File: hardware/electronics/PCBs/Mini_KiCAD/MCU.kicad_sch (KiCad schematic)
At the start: 13 parts, among them J3 HEADER2, U1 ATMEGA32U4RC-AU

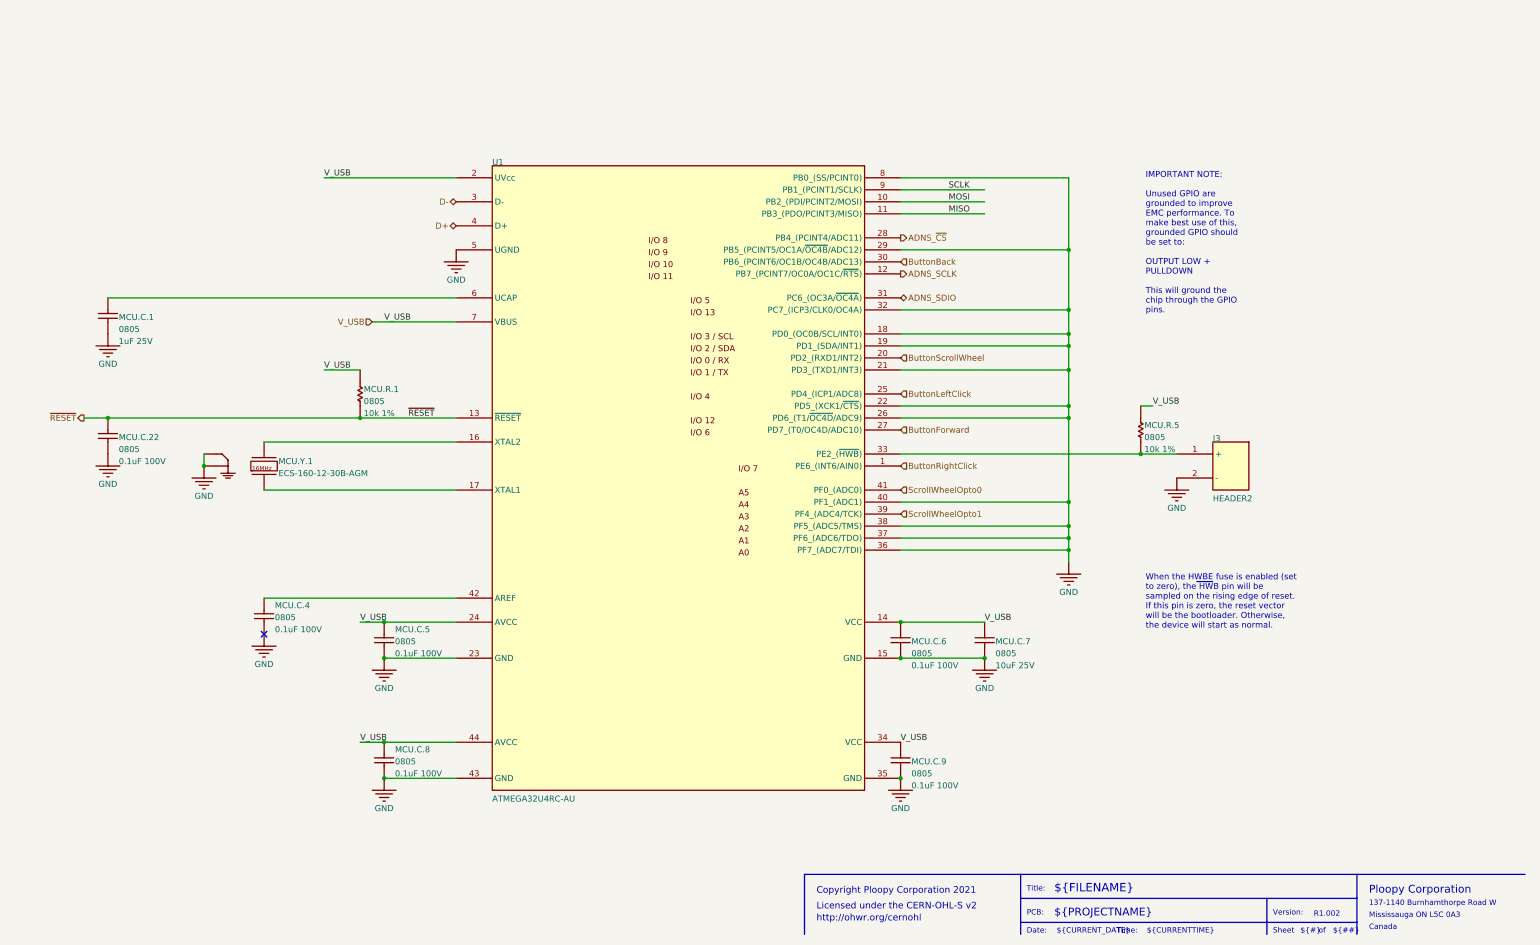
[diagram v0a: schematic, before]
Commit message: Initial commit of the modified Ploopy Mini PCB with RP2040, PMW3360 and mid-mounted USB-C
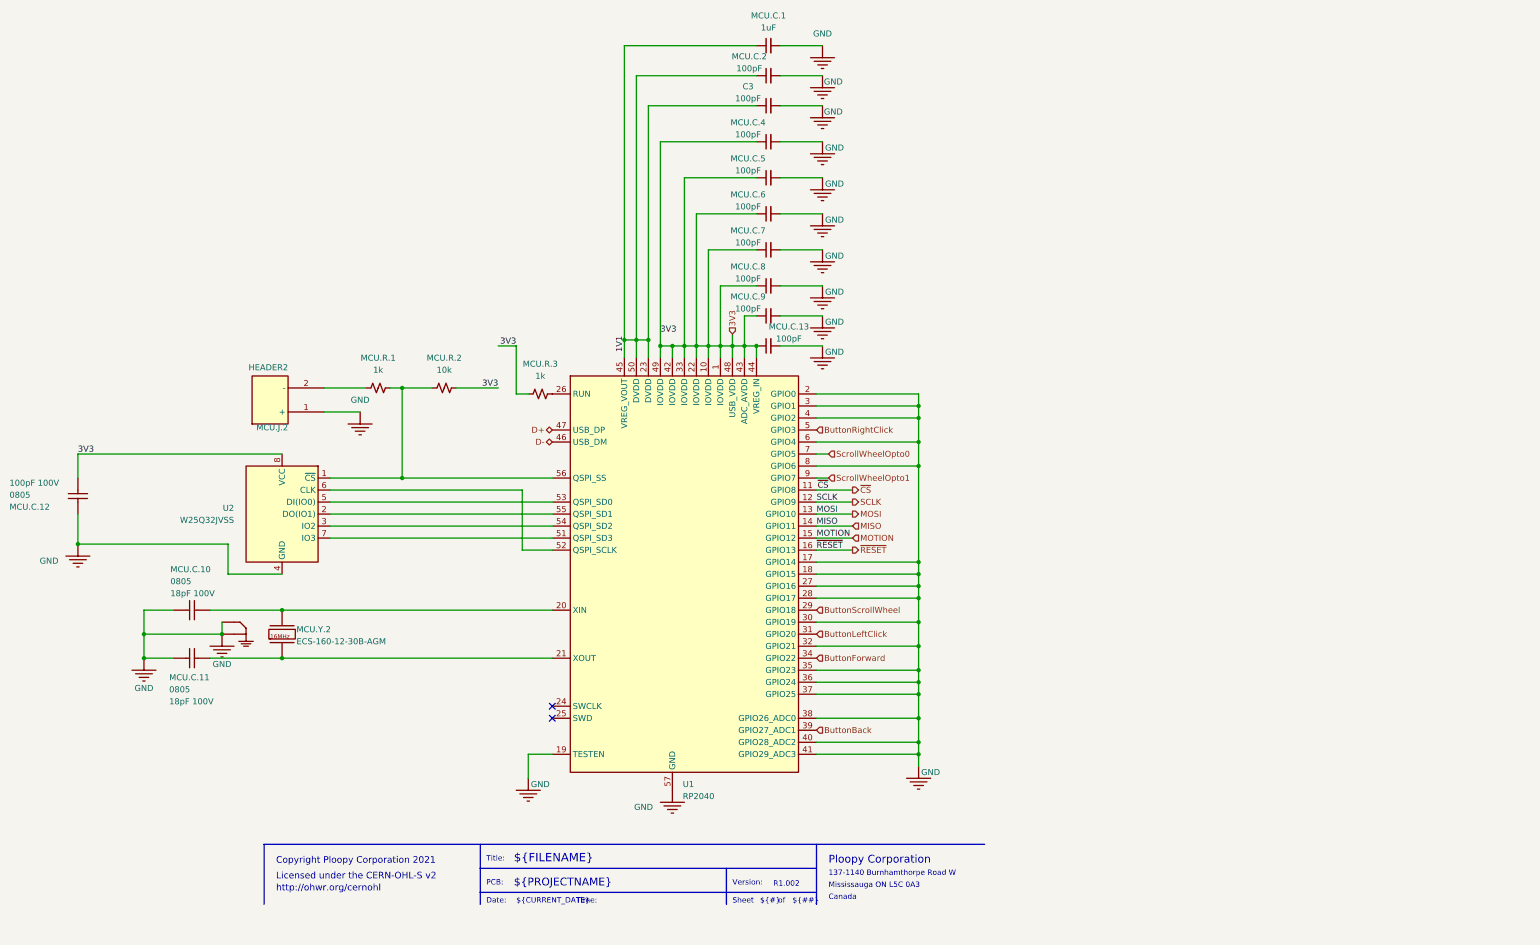
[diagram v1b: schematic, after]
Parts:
- removed J3: HEADER2, 2x1, symbol Mini-altium-import:MCU_0_HEADER2
- removed MCU.C.1: 0805, 0805 - TALL, symbol Mini-altium-import:MCU_1_Cap 1uF 25V
- removed MCU.C.22, MCU.C.4, MCU.C.5, MCU.C.8, MCU.C.9: 0805, 0805 - TALL, symbol Mini-altium-import:MCU_1_Cap 0.1uF 100V
- removed MCU.C.6: 0805, 0805 - TALL, symbol Mini-altium-import:MCU_1_mirrored_Cap 0.1uF 100V
- removed MCU.C.7: 0805, 0805 - TALL, symbol Mini-altium-import:MCU_1_mirrored_Cap 10uF 25V
- removed MCU.R.1, MCU.R.5: 0805, 0805, symbol Mini-altium-import:MCU_1_Res 10k 1% 0805
- removed MCU.Y.1: ECS-160-12-30B-AGM, LFXTAL055663BULK, symbol Mini-altium-import:MCU_0_ECS-160-12-30B-AGM
- removed U1: ATMEGA32U4RC-AU, ATmega32U4 - TQFP80P1200X1200X120-44N, symbol Mini-altium-import:MCU_0_ATMEGA32U4RC-AU
- added C3, MCU.C.13, MCU.C.2, MCU.C.4, MCU.C.5, MCU.C.6, MCU.C.7, MCU.C.8, MCU.C.9: 100pF, Chip_Passives.PcbLib:0805, symbol Device:C_Small
- added MCU.C.1: 1uF, Chip_Passives.PcbLib:0805, symbol Device:C_Small
- added MCU.C.10, MCU.C.11, MCU.C.12: 0805, Chip_Passives.PcbLib:0805 - TALL, symbol Mini-altium-import:MCU_1_Cap 0.1uF 100V
- added MCU.J.2: HEADER2, Connectors.PcbLib:2x1, symbol Mini-altium-import:MCU_0_HEADER2
- added MCU.R.1, MCU.R.3: 1k, Chip_Passives.PcbLib:0805, symbol Device:R_Small_US
- added MCU.R.2: 10k, Chip_Passives.PcbLib:0805, symbol Device:R_Small_US
- added MCU.Y.2: ECS-160-12-30B-AGM, Crystals.PcbLib:LFXTAL055663BULK, symbol Mini-altium-import:MCU_0_ECS-160-12-30B-AGM
- added U1: RP2040, Package_DFN_QFN:QFN-56-1EP_7x7mm_P0.4mm_EP3.2x3.2mm, symbol MCU_RaspberryPi:RP2040
- added U2: W25Q32JVSS, Package_SO:SOIC-8_5.23x5.23mm_P1.27mm, symbol Memory_Flash:W25Q32JVSS
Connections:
- net ButtonBack: now also U1.39 (GPIO27_ADC1)
- net ButtonForward: now also U1.34 (GPIO22)
- net ButtonLeftClick: now also U1.31 (GPIO20)
- net ButtonRightClick: now also U1.5 (GPIO3)
- net ButtonScrollWheel: now also U1.29 (GPIO18)
- net D+: now also U1.47 (USB_DP)
- net D-: now also U1.46 (USB_DM)
- net GND: now also C3.2, MCU.C.1.2, MCU.C.10.1, MCU.C.11.1, MCU.C.12.1, MCU.C.13.2, MCU.C.2.2, MCU.C.4.2, MCU.C.5.2, MCU.C.6.2, MCU.C.7.2, MCU.C.8.2, MCU.C.9.2, MCU.J.2.1 (+), MCU.Y.2.2, MCU.Y.2.4, U1.17 (GPIO14), U1.18 (GPIO15), U1.19 (TESTEN), U1.2 (GPIO0), U1.27 (GPIO16), U1.28 (GPIO17), U1.3 (GPIO1), U1.30 (GPIO19), U1.32 (GPIO21), U1.35 (GPIO23), U1.36 (GPIO24), U1.37 (GPIO25), U1.38 (GPIO26_ADC0), U1.4 (GPIO2), U1.40 (GPIO28_ADC2), U1.41 (GPIO29_ADC3), U1.57 (GND), U1.6 (GPIO4), U1.8 (GPIO6), U2.4 (GND)
- net MISO: now also U1.14 (GPIO11)
- net MOSI: now also U1.13 (GPIO10)
- net SCLK: now also U1.12 (GPIO9)
- net ScrollWheelOpto0: now also U1.7 (GPIO5)
- net ScrollWheelOpto1: now also U1.9 (GPIO7)
- net ~{RESET}: now also U1.16 (GPIO13)
- new net: MCU.R.3.2, U1.26 (RUN)
- new net: MCU.C.10.2, MCU.Y.2.1, U1.20 (XIN)
- new net: MCU.C.11.2, MCU.Y.2.3, U1.21 (XOUT)
- new net: MCU.R.1.2, MCU.R.2.1, U1.56 (QSPI_SS), U2.1 (~{CS})
- new net: U1.55 (QSPI_SD1), U2.2 (DO(IO1))
- new net: U1.54 (QSPI_SD2), U2.3 (IO2)
- new net: U1.53 (QSPI_SD0), U2.5 (DI(IO0))
- new net: U1.52 (QSPI_SCLK), U2.6 (CLK)
- new net: U1.51 (QSPI_SD3), U2.7 (IO3)
- new net: MCU.J.2.2 (-), MCU.R.1.1
- new net 1V1: C3.1, MCU.C.1.1, MCU.C.2.1, U1.23 (DVDD), U1.45 (VREG_VOUT), U1.50 (DVDD)
- new net 3V3: MCU.C.12.2, MCU.C.13.1, MCU.C.4.1, MCU.C.5.1, MCU.C.6.1, MCU.C.7.1, MCU.C.8.1, MCU.C.9.1, MCU.R.2.2, MCU.R.3.1, U1.1 (IOVDD), U1.10 (IOVDD), U1.22 (IOVDD), U1.33 (IOVDD), U1.42 (IOVDD), U1.43 (ADC_AVDD), U1.44 (VREG_IN), U1.48 (USB_VDD), U1.49 (IOVDD), U2.8 (VCC)
- new net MOTION: U1.15 (GPIO12)
- new net ~{CS}: U1.11 (GPIO8)
- no-connect marks 1 -> 2
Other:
- note removed: "${CURRENTTIME}"

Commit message: Fixed SPI pin assignment, capacitor values and added the missing resistor for the crystal
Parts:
- added MCU.R.4: 1k, Chip_Passives.PcbLib:0805, symbol Device:R_Small_US
- MCU.C.13: value 100pF -> 1uf
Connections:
- net GND: now also U1.11 (GPIO8), U1.13 (GPIO10); no longer U1.2 (GPIO0), U1.4 (GPIO2)
- net MISO: now also U1.2 (GPIO0); no longer U1.14 (GPIO11)
- net MOSI: now also U1.9 (GPIO7); no longer U1.13 (GPIO10)
- net SCLK: now also U1.4 (GPIO2); no longer U1.12 (GPIO9)
- net ScrollWheelOpto0: now also U1.14 (GPIO11); no longer U1.7 (GPIO5)
- net ScrollWheelOpto1: now also U1.12 (GPIO9); no longer U1.9 (GPIO7)
- net ~{CS}: now also U1.7 (GPIO5); no longer U1.11 (GPIO8)
- net at MCU.C.11.2, MCU.Y.2.3: now also MCU.R.4.1; no longer U1.21 (XOUT)
- new net: MCU.R.4.2, U1.21 (XOUT)

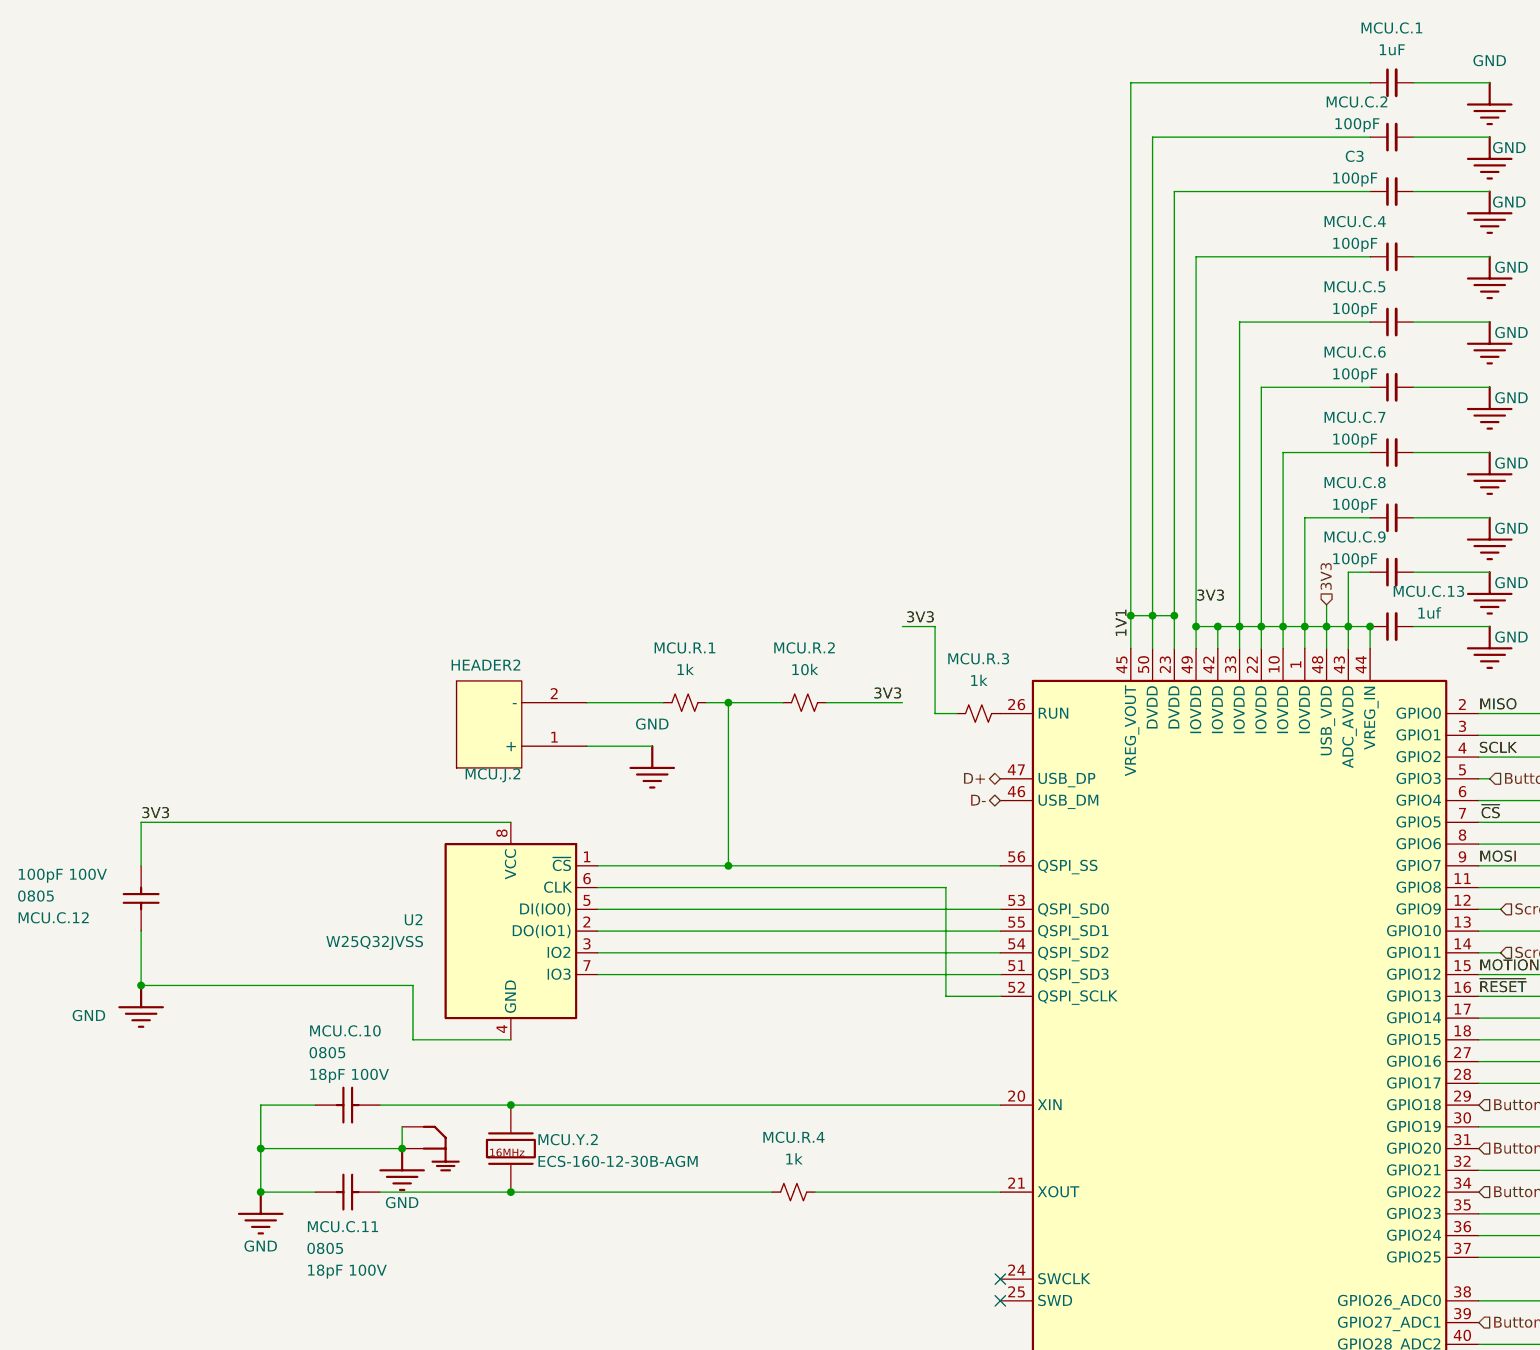
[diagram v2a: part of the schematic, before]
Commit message: Fixed crystal and capacitor values
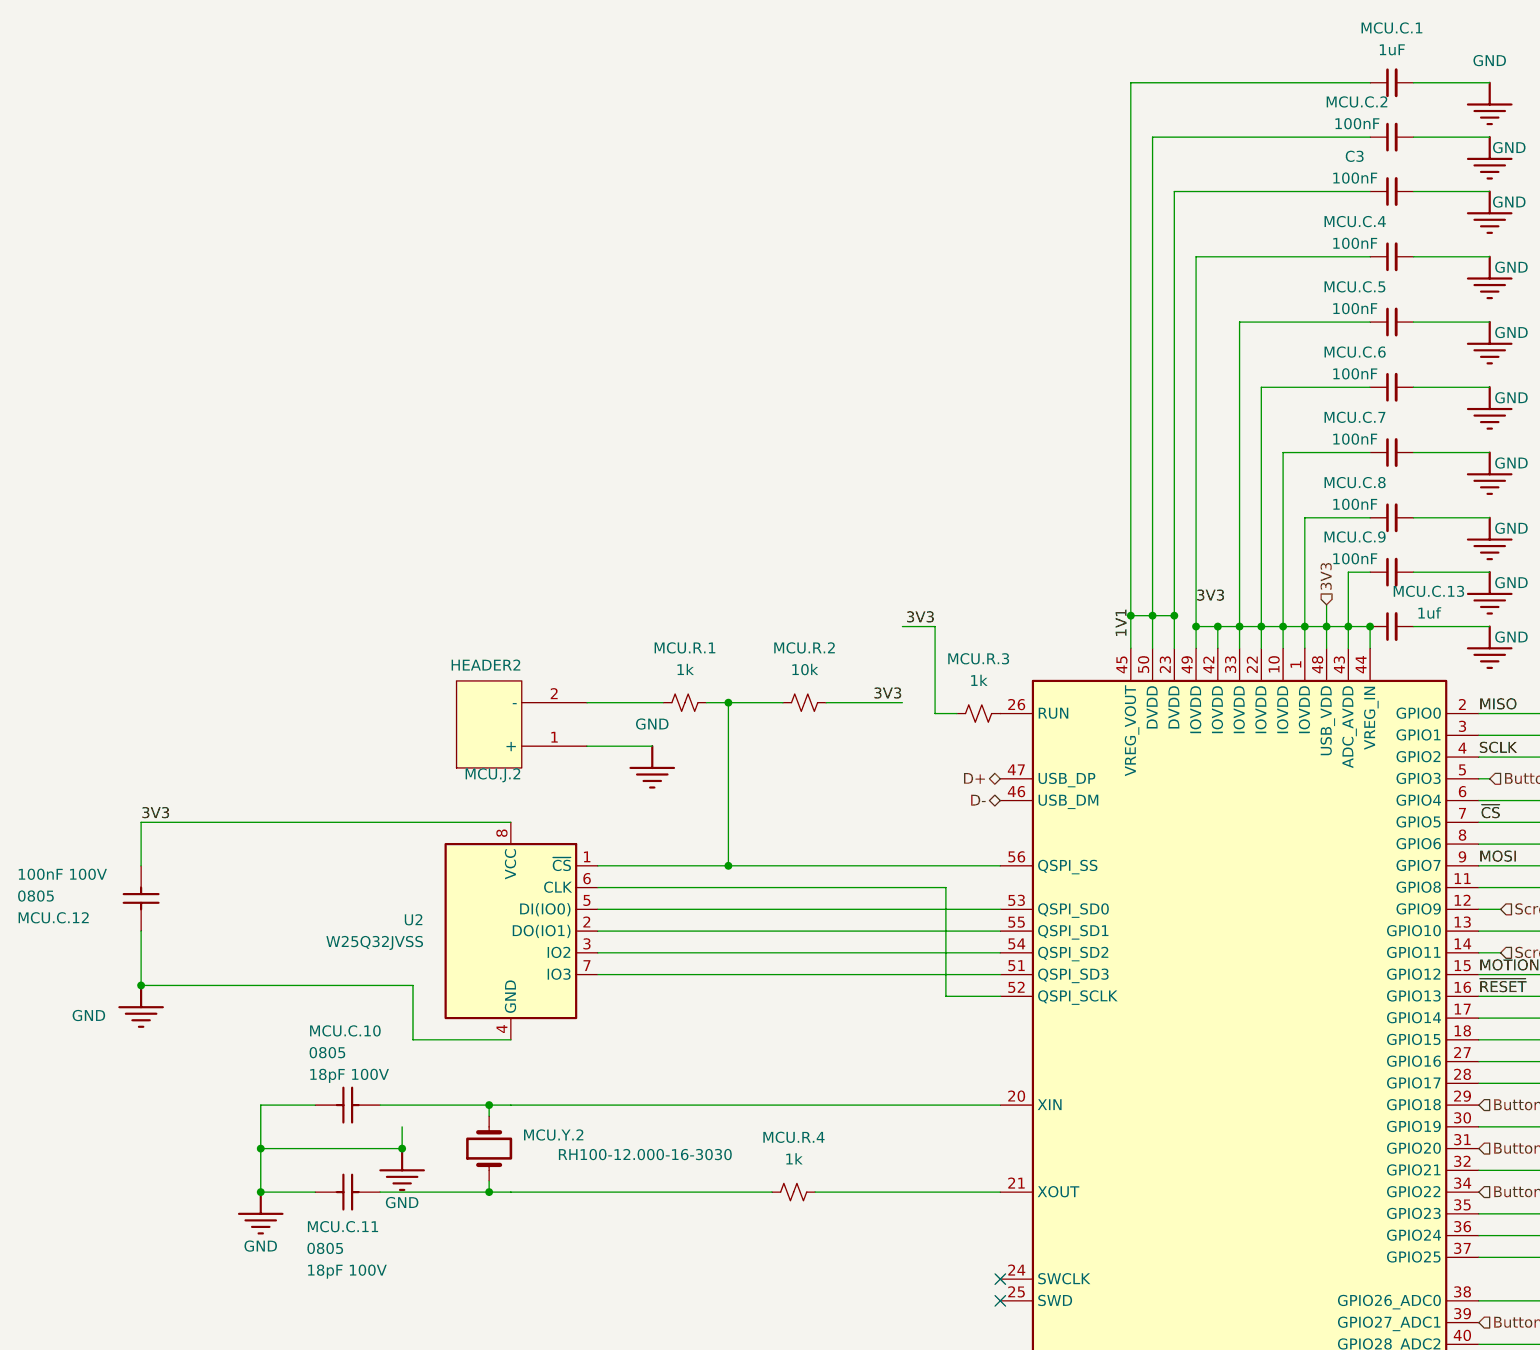
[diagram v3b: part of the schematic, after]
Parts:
- C3, MCU.C.2, MCU.C.4, MCU.C.5, MCU.C.6, MCU.C.7, MCU.C.8, MCU.C.9: value 100pF -> 100nF
- MCU.C.12: ALTIUM_VALUE 100pF 100V -> 100nF 100V
- MCU.Y.2: value ECS-160-12-30B-AGM -> RH100-12.000-16-3030; symbol Mini-altium-import:MCU_0_ECS-160-12-30B-AGM -> Device:Crystal
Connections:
- net GND: no longer MCU.Y.2.2, MCU.Y.2.4
- net at MCU.C.10.2, U1.20 (XIN): now also MCU.Y.2.2; no longer MCU.Y.2.1
- net at MCU.C.11.2, MCU.R.4.1: now also MCU.Y.2.1; no longer MCU.Y.2.3
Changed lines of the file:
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@@
 	)
 	(junction
+		(at 85.09 142.24)
+		(diameter 0)
+		(color 0 0 0 0)
+	)
+	(junction
 		(at 187.96 86.36)
 		(diameter 0)
@@
 	)
 	(junction
-		(at 87.63 142.24)
-		(diameter 0)
-		(color 0 0 0 0)
-	)
-	(junction
 		(at 222.25 139.7)
 		(diameter 0)
@@
 	)
 	(junction
-		(at 222.25 144.78)
+		(at 85.09 152.4)
 		(diameter 0)
 		(color 0 0 0 0)
 	)
 	(junction
-		(at 87.63 152.4)
+		(at 222.25 144.78)
 		(diameter 0)
 		(color 0 0 0 0)
@@
 	(wire
 		(pts
+			(xy 85.09 151.13) (xy 85.09 152.4)
+		)
+		(stroke
+			(width 0)
+			(type default)
+		)
+	)
+	(wire
+		(pts
 			(xy 167.64 86.36) (xy 167.64 88.9)
 		)
@@
 	(wire
 		(pts
+			(xy 85.09 142.24) (xy 85.09 143.51)
+		)
+		(stroke
+			(width 0)
+			(type default)
+		)
+	)
+	(wire
+		(pts
 			(xy 193.04 50.8) (xy 201.93 50.8)
 		)
@@
 	(wire
 		(pts
+			(xy 85.09 142.24) (xy 87.63 142.24)
+		)
+		(stroke
+			(width 0)
+			(type default)
+		)
+	)
+	(wire
+		(pts
+			(xy 85.09 152.4) (xy 87.63 152.4)
+		)
+		(stroke
+			(width 0)
+			(type default)
+		)
+	)
+	(wire
+		(pts
 			(xy 113.03 95.25) (xy 113.03 114.3)
 		)
@@
 	(wire
 		(pts
-			(xy 72.39 142.24) (xy 87.63 142.24)
+			(xy 72.39 142.24) (xy 85.09 142.24)
 		)
 		(stroke
@@
 	(wire
 		(pts
-			(xy 72.39 152.4) (xy 87.63 152.4)
+			(xy 72.39 152.4) (xy 85.09 152.4)
 		)
 		(stroke
@@
 			)
 		)
-		(property "Value" "100pF"
+		(property "Value" "100nF"
 			(at 186.182 72.136 90)
 			(effects
@@
 	)
 	(symbol
-		(lib_id "Mini-altium-import:MCU_0_ECS-160-12-30B-AGM")
-		(at 85.09 147.32 0)
+		(lib_id "Device:Crystal")
+		(at 85.09 147.32 90)
 		(unit 1)
 		(exclude_from_sim no)
@@
 		(dnp no)
 		(property "Reference" "MCU.Y.2"
-			(at 90.678 147.066 0)
+			(at 96.266 145.034 90)
 			(effects
 				(font
@@
 			)
 		)
-		(property "Value" "ECS-160-12-30B-AGM"
-			(at 90.678 149.606 0)
+		(property "Value" "RH100-12.000-16-3030"
+			(at 113.538 147.32 90)
 			(effects
 				(font
@@
 			)
 		)
-		(property "Datasheet" ""
+		(property "Datasheet" "~"
 			(at 85.09 147.32 0)
 			(effects
@@
 			)
 		)
-		(property "Description" ""
+		(property "Description" "Two pin crystal"
 			(at 85.09 147.32 0)
 			(effects
@@
 		)
 		(property "SUPPLIER 1" "Digi-Key"
-			(at 74.422 141.732 0)
+			(at 79.502 157.988 0)
 			(effects
 				(font
@@
 		)
 		(property "SUPPLIER 2" "Mouser"
-			(at 74.422 139.192 0)
+			(at 76.962 157.988 0)
 			(effects
 				(font
@@
 		)
 		(property "SUPPLIER PART NUMBER 1" "XC2686CT-ND"
-			(at 74.422 141.732 0)
+			(at 79.502 157.988 0)
 			(effects
 				(font
@@
 		)
 		(property "SUPPLIER PART NUMBER 2" "520-160-12-30B-AGMT"
-			(at 74.422 139.192 0)
+			(at 76.962 157.988 0)
 			(effects
 				(font
@@
 		(pin "1"
 		)
-		(pin "4"
-		)
-		(pin "3"
-		)
 		(pin "2"
 		)
@@
 			)
 		)
-		(property "Value" "100pF"
+		(property "Value" "100nF"
 			(at 186.182 41.656 90)
 			(effects
@@
 			)
 		)
-		(property "Value" "100pF"
+		(property "Value" "100nF"
 			(at 186.182 49.276 90)
 			(effects
@@
 			)
 		)
-		(property "Value" "100pF"
+		(property "Value" "100nF"
 			(at 186.436 27.686 90)
 			(effects
@@
 			)
 		)
-		(property "Value" "100pF"
+		(property "Value" "100nF"
 			(at 186.182 56.896 90)
 			(effects
@@
 			)
 		)
-		(property "Value" "100pF"
+		(property "Value" "100nF"
 			(at 186.182 64.516 90)
 			(effects
@@
 			)
 		)
-		(property "Value" "100pF"
+		(property "Value" "100nF"
 			(at 186.182 34.036 90)
 			(effects
@@
 			)
 		)
-		(property "Value" "100pF"
+		(property "Value" "100nF"
 			(at 186.182 78.486 90)
 			(effects
@@
 			)
 		)
-		(property "ALTIUM_VALUE" "100pF 100V"
+		(property "ALTIUM_VALUE" "100nF 100V"
 			(at 29.972 116.078 0)
 			(effects
